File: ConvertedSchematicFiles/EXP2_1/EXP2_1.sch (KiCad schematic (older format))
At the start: 9 parts

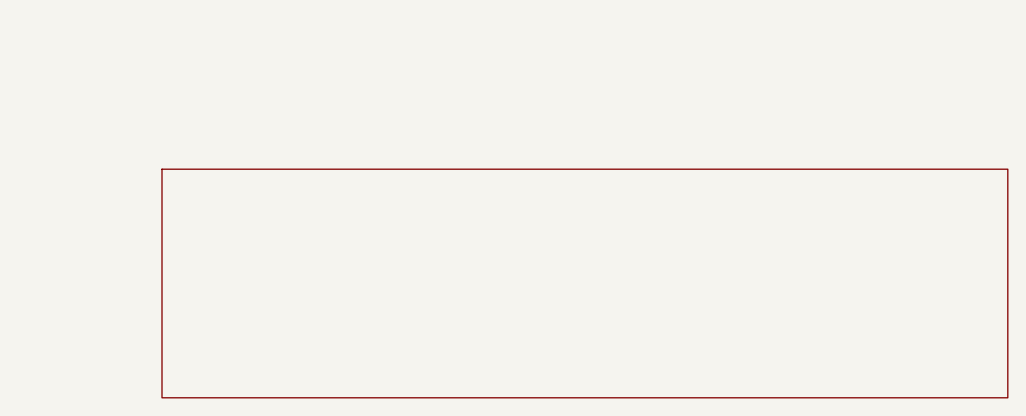
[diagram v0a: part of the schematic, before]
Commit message: Excluded some components. These no longer appear after conversion. When calling shell commands, filenames are in "quotes"
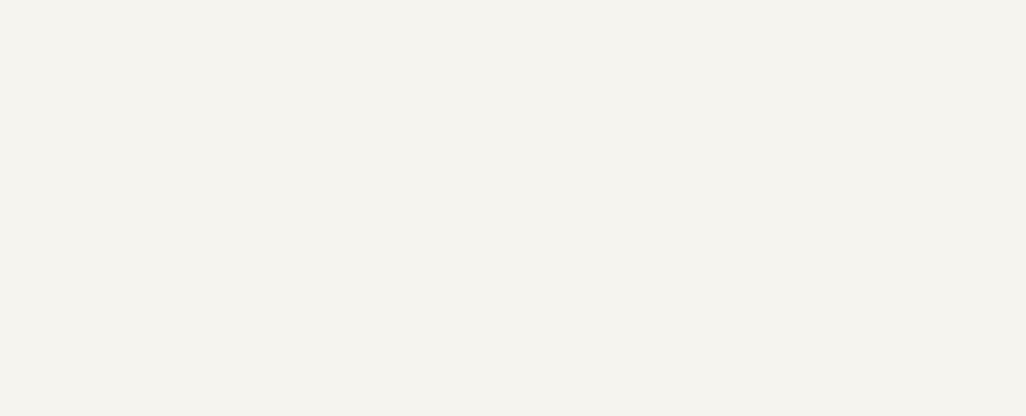
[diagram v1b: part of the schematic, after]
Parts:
- removed titleblk: titleblk, symbol TITLEBLK_PSPICE
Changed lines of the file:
@@
 	0    1    -1    0
-$EndComp
-$Comp
-L TITLEBLK_PSPICE titleblk
-U 1 1 66516649
-P 11880 8400
-F 0 "titleblk" H 23760 16800 30  0001 L CNN
-F 1 "titleblk" H 23760 16880 30  0001 L CNN
-	1    11880 8400
-	1    0    0    1
 $EndComp
 Wire Wire Line

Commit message: Ports issue fixed. Now annotation for ports is #PWR? function added "itos"
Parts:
- removed EGND (x2): EGND, symbol EGND_PSPICE
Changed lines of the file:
@@
 $EndDescr
 $Comp
-L EGND_PSPICE EGND
+L EGND_PSPICE #PWR1
 U 1 1 14289383
 P 2300 1300
-F 0 "EGND" H 4600 2600 30  0001 L CNN
+F 0 "#PWR1" H 4600 2600 30  0001 L CNN
 F 1 "EGND" H 4600 2680 30  0001 L CNN
 	1    2300 1300
@@
 $EndComp
 $Comp
-L EGND_PSPICE EGND
+L EGND_PSPICE #PWR2
 U 1 1 46930886
 P 4100 1600
-F 0 "EGND" H 8200 3200 30  0001 L CNN
+F 0 "#PWR2" H 8200 3200 30  0001 L CNN
 F 1 "EGND" H 8200 3280 30  0001 L CNN
 	1    4100 1600

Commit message: Added LICENSE.txt
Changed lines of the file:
@@
 $EndDescr
 $Comp
-L EGND_PSPICE #PWR1
+L GND #PWR1
 U 1 1 14289383
 P 2300 1300
@@
 $EndComp
 $Comp
-L EGND_PSPICE #PWR2
+L GND #PWR2
 U 1 1 46930886
 P 4100 1600

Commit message: Orientation fix. Library components are now inverted, with +ve y axis going up. In Schematic files, +ve y axis is downwards. This is how the KiCad libraries are. As a result of the above fixed, the converted GND is now oriented correctly.
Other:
- moved on the sheet: V1, V2
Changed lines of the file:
@@
 F 1 "EGND" H 4600 2680 30  0001 L CNN
 	1    2300 1300
-	1    0    0    1
+	1    0    0    -1
 $EndComp
 $Comp
@@
 F 1 "EGND" H 8200 3280 30  0001 L CNN
 	1    4100 1600
-	1    0    0    1
+	1    0    0    -1
 $EndComp
 $Comp
@@
 F 1 "100" H 800 850 30  0000 L CNN
 	1    800 700
-	1    0    0    1
+	1    0    0    -1
 $EndComp
 $Comp
@@
 F 1 "50" H 1600 850 30  0000 L CNN
 	1    1600 700
-	1    0    0    1
+	1    0    0    -1
 $EndComp
 $Comp
@@
 F 1 "10V" H 1200 1190 30  0000 C CNN
 	1    1200 1300
-	0    1    -1    0
+	0    -1    -1    0
 $EndComp
 $Comp
@@
 F 1 "50" H 3300 1250 30  0000 L CNN
 	1    3300 1100
-	1    0    0    1
+	1    0    0    -1
 $EndComp
 $Comp
@@
 F 1 "100" H 3300 750 30  0000 L CNN
 	1    3300 600
-	1    0    0    1
+	1    0    0    -1
 $EndComp
 $Comp
@@
 F 1 "10V" H 3300 1490 30  0000 C CNN
 	1    3300 1600
-	0    1    -1    0
+	0    -1    -1    0
 $EndComp
 Wire Wire Line

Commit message: Removed the use of exec, wrote basename function, made integration with eSim easier.
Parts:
- added titleblk: titleblk, symbol titleblk_PSPICE
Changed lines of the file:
@@
-EESchema Schematic File Version 2  date Thursday 24 February 2000 08:27:28 PM IST
+EESchema Schematic File Version 2  date
 LIBS:power
 LIBS:device
@@
 LIBS:contrib
 LIBS:valves
-LIBS:ConvertedSchematicFiles/EXP2_1-cache
 EELAYER 25  0
 EELAYER END
@@
 Sheet 1 1
 Title ""
-Date "24 Feb 2000"
+Date ""
 Rev ""
 Comp ""
@@
 	0    -1    -1    0
 $EndComp
+$Comp
+L titleblk_PSPICE titleblk
+U 1 1 66516649
+P 11880 8400
+F 0 "titleblk" H 23760 16800 30  0001 L CNN
+F 1 "titleblk" H 23760 16880 30  0001 L CNN
+	1    11880 8400
+	1    0    0    -1
+$EndComp
 Wire Wire Line
